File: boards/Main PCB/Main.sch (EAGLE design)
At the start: 98 parts, among them CN1 MINIB, CN2 MINIB, IC1 FT232RL, IC2 FT232RL, J1 3_PIN_JST-XH, J2 2_PIN_JST-XH, Q4 BSS138, Q5 BSS138, Q6 BSS138, Q7 BSS138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

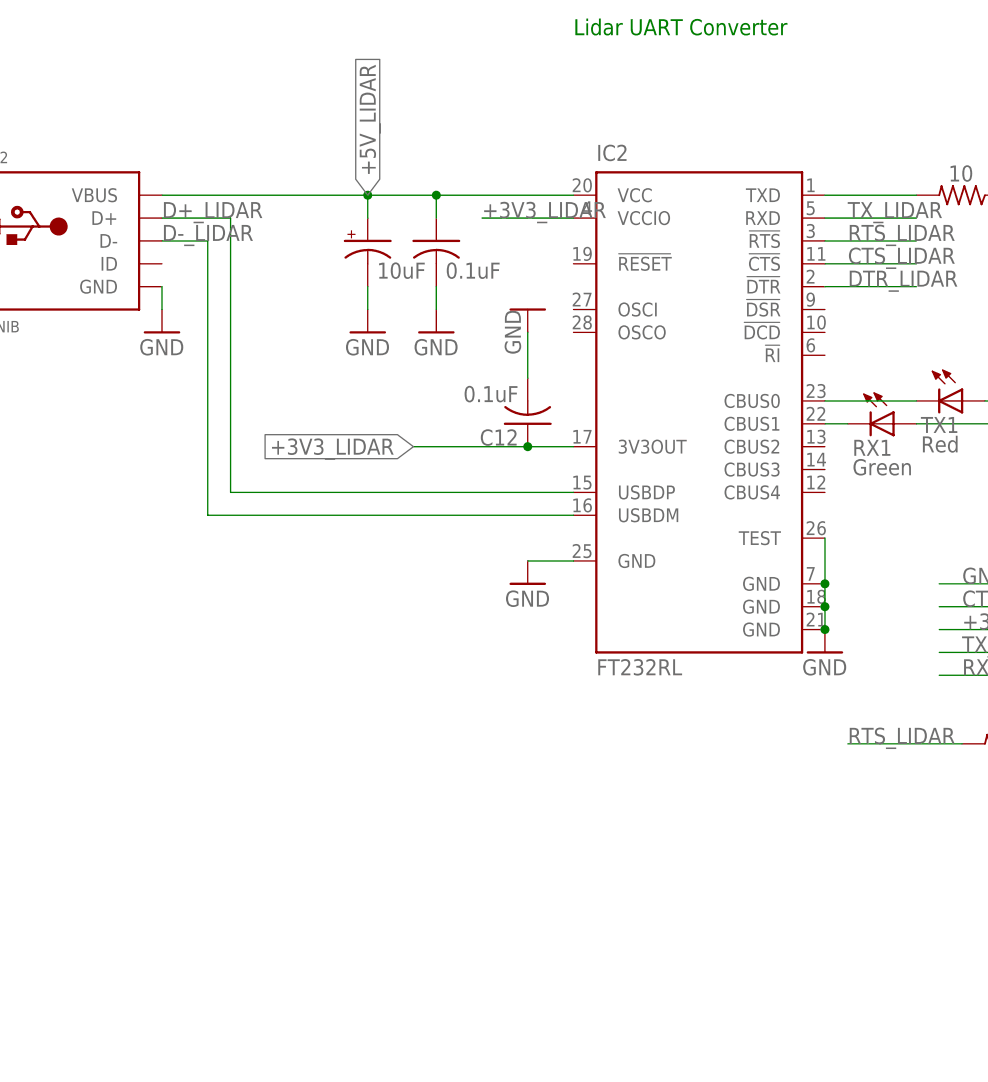
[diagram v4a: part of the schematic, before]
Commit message: Adding diode for lidar protection
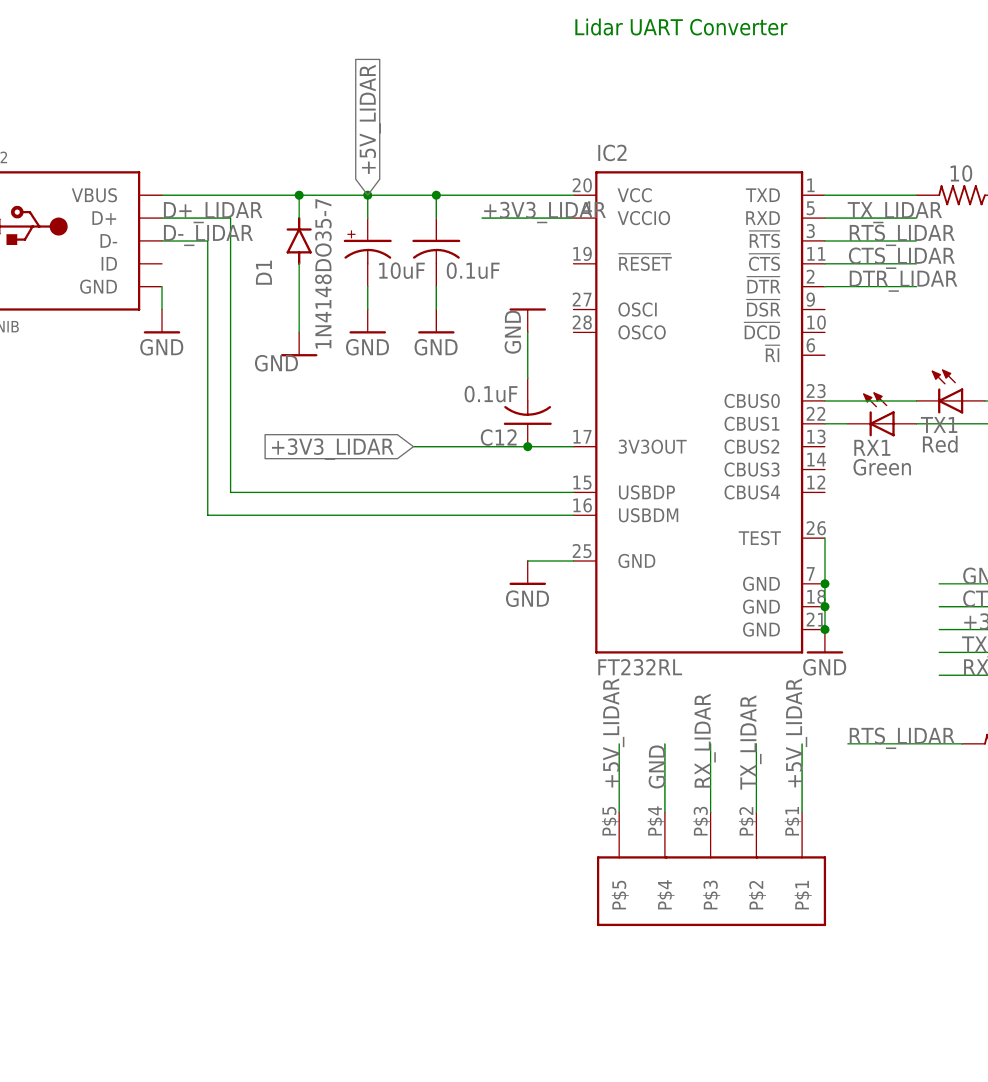
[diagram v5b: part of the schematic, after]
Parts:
- added D1: 1N4148DO35-7, diode:1N4148DO35-7
- added J3: 5_PIN_JST-XH, main_library:5_PIN_JST-XH
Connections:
- net +5V_LIDAR: now also D1.C, J3.P$1, J3.P$5
- net GND: now also D1.A, J3.P$4
- net RX_LIDAR: now also J3.P$3
- net TX_LIDAR: now also J3.P$2
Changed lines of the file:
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@@
 <?xml version="1.0" encoding="utf-8"?>
 <!DOCTYPE eagle SYSTEM "eagle.dtd">
-<eagle version="9.2.2">
+<eagle version="9.3.0">
 <drawing>
 <settings>
@@
 <part name="U$6" library="microbuilder" deviceset="GND" device=""/>
 <part name="R33" library="RESET_FUSE" deviceset="0ZCJ0050FF2G" device=""/>
+<part name="J3" library="main_library" deviceset="5_PIN_JST-XH" device=""/>
+<part name="D1" library="diode" library_urn="urn:adsk.eagle:library:210" deviceset="1N4148" device="DO35-7" package3d_urn="urn:adsk.eagle:package:43339/1"/>
+<part name="GND34" library="supply1" library_urn="urn:adsk.eagle:library:371" deviceset="GND" device=""/>
 </parts>
 <sheets>
@@
 <attribute name="NAME" x="316.23" y="385.0386" size="1.778" layer="95"/>
 <attribute name="VALUE" x="316.23" y="380.238" size="1.778" layer="96"/>
+</instance>
+<instance part="J3" gate="G$1" x="241.3" y="58.42" smashed="yes" rot="R270"/>
+<instance part="D1" gate="G$1" x="195.58" y="129.54" smashed="yes" rot="R90">
+<attribute name="NAME" x="192.5574" y="124.46" size="1.778" layer="95" rot="R90"/>
+<attribute name="VALUE" x="199.1614" y="117.348" size="1.778" layer="96" rot="R90"/>
+</instance>
+<instance part="GND34" gate="1" x="195.58" y="116.84" smashed="yes">
+<attribute name="VALUE" x="195.58" y="116.84" size="1.778" layer="96" rot="R180"/>
 </instance>
 </instances>
@@
 <pinref part="U$6" gate="G$1" pin="GND"/>
 </segment>
+<segment>
+<pinref part="J3" gate="G$1" pin="P$4"/>
+<wire x1="236.22" y1="66.04" x2="236.22" y2="73.66" width="0.1524" layer="91"/>
+<label x="236.22" y="68.58" size="1.778" layer="95" rot="R90"/>
+</segment>
+<segment>
+<pinref part="GND34" gate="1" pin="GND"/>
+<pinref part="D1" gate="G$1" pin="A"/>
+<wire x1="195.58" y1="119.38" x2="195.58" y2="127" width="0.1524" layer="91"/>
+</segment>
 </net>
 <net name="N$36" class="0">
@@
 <wire x1="203.2" y1="132.08" x2="203.2" y2="134.62" width="0.1524" layer="91"/>
 <wire x1="210.82" y1="132.08" x2="210.82" y2="134.62" width="0.1524" layer="91"/>
-<wire x1="203.2" y1="134.62" x2="180.34" y2="134.62" width="0.1524" layer="91"/>
+<wire x1="203.2" y1="134.62" x2="195.58" y2="134.62" width="0.1524" layer="91"/>
 <junction x="203.2" y="134.62"/>
 <junction x="210.82" y="134.62"/>
@@
 <pinref part="CN2" gate="G$1" pin="VBUS"/>
 <label x="203.2" y="134.62" size="1.778" layer="95" rot="R90" xref="yes"/>
+<pinref part="D1" gate="G$1" pin="C"/>
+<wire x1="195.58" y1="134.62" x2="180.34" y2="134.62" width="0.1524" layer="91"/>
+<wire x1="195.58" y1="132.08" x2="195.58" y2="134.62" width="0.1524" layer="91"/>
+<junction x="195.58" y="134.62"/>
+</segment>
+<segment>
+<pinref part="J3" gate="G$1" pin="P$1"/>
+<wire x1="251.46" y1="66.04" x2="251.46" y2="73.66" width="0.1524" layer="91"/>
+<label x="251.46" y="68.58" size="1.778" layer="95" rot="R90"/>
+</segment>
+<segment>
+<pinref part="J3" gate="G$1" pin="P$5"/>
+<wire x1="231.14" y1="66.04" x2="231.14" y2="73.66" width="0.1524" layer="91"/>
+<label x="231.14" y="68.58" size="1.778" layer="95" rot="R90"/>
 </segment>
 </net>
@@
 <pinref part="FTDI1" gate="A" pin="5"/>
 </segment>
+<segment>
+<pinref part="J3" gate="G$1" pin="P$3"/>
+<wire x1="241.3" y1="66.04" x2="241.3" y2="73.66" width="0.1524" layer="91"/>
+<label x="241.3" y="68.58" size="1.778" layer="95" rot="R90"/>
+</segment>
 </net>
 <net name="TX_LIDAR" class="0">
@@
 <pinref part="FTDI1" gate="A" pin="4"/>
 </segment>
-</net>
+<segment>
+<pinref part="J3" gate="G$1" pin="P$2"/>
+<wire x1="246.38" y1="66.04" x2="246.38" y2="73.66" width="0.1524" layer="91"/>
+<label x="246.38" y="68.58" size="1.778" layer="95" rot="R90"/>
+</segment>
+</net>

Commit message: Fixing trace widths and net names
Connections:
- net N$11 renamed CAP
- net N$13 renamed LED
- net N$34 renamed BOOT0
- net N$43 renamed RESET
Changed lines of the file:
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@@
 <?xml version="1.0" encoding="utf-8"?>
 <!DOCTYPE eagle SYSTEM "eagle.dtd">
-<eagle version="9.3.0">
+<eagle version="9.2.2">
 <drawing>
 <settings>
@@
 </segment>
 </net>
-<net name="N$34" class="0">
+<net name="BOOT0" class="0">
 <segment>
 <pinref part="U2" gate="G$1" pin="BOOT0"/>
@@
 </segment>
 </net>
-<net name="N$43" class="0">
+<net name="RESET" class="0">
 <segment>
 <wire x1="220.98" y1="297.18" x2="220.98" y2="325.12" width="0.1524" layer="91"/>
@@
 </segment>
 </net>
-<net name="N$13" class="0">
+<net name="LED" class="0">
 <segment>
 <pinref part="RX2" gate="G$1" pin="C"/>
@@
 </segment>
 </net>
-<net name="N$11" class="0">
+<net name="CAP" class="0">
 <segment>
 <pinref part="U$3" gate="G$1" pin="CAP"/>

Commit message: AAdding decoupling capacitors for design review
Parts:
- added C18, C19, C26, C27, C28, C29: .1uF, rcl:C-USC0805
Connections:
- net +3V3: now also C28.1, C29.1
- net +5V: now also C18.1, C19.1, C26.1, C27.1
- net GND: now also C18.2, C19.2, C26.2, C27.2, C28.2, C29.2
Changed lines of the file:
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@@
 <part name="D1" library="diode" library_urn="urn:adsk.eagle:library:210" deviceset="1N4148" device="DO35-7" package3d_urn="urn:adsk.eagle:package:43339/1"/>
 <part name="GND34" library="supply1" library_urn="urn:adsk.eagle:library:371" deviceset="GND" device=""/>
+<part name="C18" library="rcl" library_urn="urn:adsk.eagle:library:334" deviceset="C-US" device="C0805" package3d_urn="urn:adsk.eagle:package:23617/2" value=".1uF"/>
+<part name="C19" library="rcl" library_urn="urn:adsk.eagle:library:334" deviceset="C-US" device="C0805" package3d_urn="urn:adsk.eagle:package:23617/2" value=".1uF"/>
+<part name="C26" library="rcl" library_urn="urn:adsk.eagle:library:334" deviceset="C-US" device="C0805" package3d_urn="urn:adsk.eagle:package:23617/2" value=".1uF"/>
+<part name="C28" library="rcl" library_urn="urn:adsk.eagle:library:334" deviceset="C-US" device="C0805" package3d_urn="urn:adsk.eagle:package:23617/2" value=".1uF"/>
+<part name="C29" library="rcl" library_urn="urn:adsk.eagle:library:334" deviceset="C-US" device="C0805" package3d_urn="urn:adsk.eagle:package:23617/2" value=".1uF"/>
+<part name="GND35" library="supply1" library_urn="urn:adsk.eagle:library:371" deviceset="GND" device=""/>
+<part name="GND36" library="supply1" library_urn="urn:adsk.eagle:library:371" deviceset="GND" device=""/>
+<part name="GND37" library="supply1" library_urn="urn:adsk.eagle:library:371" deviceset="GND" device=""/>
+<part name="GND38" library="supply1" library_urn="urn:adsk.eagle:library:371" deviceset="GND" device=""/>
+<part name="GND39" library="supply1" library_urn="urn:adsk.eagle:library:371" deviceset="GND" device=""/>
+<part name="C27" library="rcl" library_urn="urn:adsk.eagle:library:334" deviceset="C-US" device="C0805" package3d_urn="urn:adsk.eagle:package:23617/2" value=".1uF"/>
+<part name="GND40" library="supply1" library_urn="urn:adsk.eagle:library:371" deviceset="GND" device=""/>
 </parts>
 <sheets>
@@
 <instance part="GND34" gate="1" x="195.58" y="116.84" smashed="yes">
 <attribute name="VALUE" x="195.58" y="116.84" size="1.778" layer="96" rot="R180"/>
+</instance>
+<instance part="C18" gate="G$1" x="45.72" y="360.68" smashed="yes" rot="R270">
+<attribute name="VALUE" x="41.529" y="359.664" size="1.778" layer="96" rot="R270"/>
+</instance>
+<instance part="C19" gate="G$1" x="45.72" y="312.42" smashed="yes" rot="R270">
+<attribute name="VALUE" x="41.529" y="311.404" size="1.778" layer="96" rot="R270"/>
+</instance>
+<instance part="C26" gate="G$1" x="45.72" y="266.7" smashed="yes" rot="R270">
+<attribute name="VALUE" x="41.529" y="265.684" size="1.778" layer="96" rot="R270"/>
+</instance>
+<instance part="C28" gate="G$1" x="480.06" y="312.42" smashed="yes" rot="R90">
+<attribute name="VALUE" x="484.251" y="313.436" size="1.778" layer="96" rot="R90"/>
+</instance>
+<instance part="C29" gate="G$1" x="480.06" y="335.28" smashed="yes" rot="R90">
+<attribute name="VALUE" x="484.251" y="336.296" size="1.778" layer="96" rot="R90"/>
+</instance>
+<instance part="GND35" gate="1" x="35.56" y="266.7" smashed="yes" rot="R270">
+<attribute name="VALUE" x="33.02" y="269.24" size="1.778" layer="96" rot="R270"/>
+</instance>
+<instance part="GND36" gate="1" x="35.56" y="312.42" smashed="yes" rot="R270">
+<attribute name="VALUE" x="33.02" y="314.96" size="1.778" layer="96" rot="R270"/>
+</instance>
+<instance part="GND37" gate="1" x="35.56" y="360.68" smashed="yes" rot="R270">
+<attribute name="VALUE" x="33.02" y="363.22" size="1.778" layer="96" rot="R270"/>
+</instance>
+<instance part="GND38" gate="1" x="490.22" y="335.28" smashed="yes" rot="R90">
+<attribute name="VALUE" x="492.76" y="332.74" size="1.778" layer="96" rot="R90"/>
+</instance>
+<instance part="GND39" gate="1" x="490.22" y="312.42" smashed="yes" rot="R90">
+<attribute name="VALUE" x="492.76" y="309.88" size="1.778" layer="96" rot="R90"/>
+</instance>
+<instance part="C27" gate="G$1" x="528.32" y="261.62" smashed="yes" rot="R180">
+<attribute name="VALUE" x="527.304" y="265.811" size="1.778" layer="96" rot="R180"/>
+</instance>
+<instance part="GND40" gate="1" x="533.4" y="266.7" smashed="yes" rot="R90">
+<attribute name="VALUE" x="535.94" y="264.16" size="1.778" layer="96" rot="R90"/>
 </instance>
 </instances>
@@
 <pinref part="X6" gate="-1" pin="S"/>
 <wire x1="462.28" y1="330.2" x2="467.36" y2="330.2" width="0.1524" layer="91"/>
+<pinref part="C29" gate="G$1" pin="1"/>
+<wire x1="467.36" y1="330.2" x2="467.36" y2="335.28" width="0.1524" layer="91"/>
+<wire x1="467.36" y1="335.28" x2="477.52" y2="335.28" width="0.1524" layer="91"/>
+<junction x="467.36" y="330.2"/>
 </segment>
 <segment>
@@
 <pinref part="X7" gate="-1" pin="S"/>
 <wire x1="462.28" y1="307.34" x2="467.36" y2="307.34" width="0.1524" layer="91"/>
+<pinref part="C28" gate="G$1" pin="1"/>
+<wire x1="467.36" y1="307.34" x2="467.36" y2="312.42" width="0.1524" layer="91"/>
+<wire x1="467.36" y1="312.42" x2="477.52" y2="312.42" width="0.1524" layer="91"/>
+<junction x="467.36" y="307.34"/>
 </segment>
 <segment>
@@
 <wire x1="195.58" y1="119.38" x2="195.58" y2="127" width="0.1524" layer="91"/>
 </segment>
+<segment>
+<pinref part="GND37" gate="1" pin="GND"/>
+<pinref part="C18" gate="G$1" pin="2"/>
+<wire x1="38.1" y1="360.68" x2="40.64" y2="360.68" width="0.1524" layer="91"/>
+</segment>
+<segment>
+<pinref part="GND36" gate="1" pin="GND"/>
+<pinref part="C19" gate="G$1" pin="2"/>
+<wire x1="38.1" y1="312.42" x2="40.64" y2="312.42" width="0.1524" layer="91"/>
+</segment>
+<segment>
+<pinref part="GND35" gate="1" pin="GND"/>
+<pinref part="C26" gate="G$1" pin="2"/>
+<wire x1="38.1" y1="266.7" x2="40.64" y2="266.7" width="0.1524" layer="91"/>
+</segment>
+<segment>
+<pinref part="C29" gate="G$1" pin="2"/>
+<pinref part="GND38" gate="1" pin="GND"/>
+<wire x1="485.14" y1="335.28" x2="487.68" y2="335.28" width="0.1524" layer="91"/>
+</segment>
+<segment>
+<pinref part="C28" gate="G$1" pin="2"/>
+<pinref part="GND39" gate="1" pin="GND"/>
+<wire x1="485.14" y1="312.42" x2="487.68" y2="312.42" width="0.1524" layer="91"/>
+</segment>
+<segment>
+<pinref part="C27" gate="G$1" pin="2"/>
+<pinref part="GND40" gate="1" pin="GND"/>
+<wire x1="528.32" y1="266.7" x2="530.86" y2="266.7" width="0.1524" layer="91"/>
+</segment>
 </net>
 <net name="N$36" class="0">
@@
 <pinref part="R28" gate="G$1" pin="2"/>
 <wire x1="66.04" y1="365.76" x2="66.04" y2="360.68" width="0.1524" layer="91"/>
-<wire x1="53.34" y1="365.76" x2="53.34" y2="350.52" width="0.1524" layer="91"/>
+<wire x1="53.34" y1="365.76" x2="53.34" y2="360.68" width="0.1524" layer="91"/>
 <junction x="53.34" y="365.76"/>
+<wire x1="53.34" y1="360.68" x2="53.34" y2="350.52" width="0.1524" layer="91"/>
 <wire x1="53.34" y1="350.52" x2="50.8" y2="350.52" width="0.1524" layer="91"/>
 <pinref part="X3" gate="-4" pin="S"/>
 <pinref part="P+3" gate="1" pin="+5V"/>
+<pinref part="C18" gate="G$1" pin="1"/>
+<wire x1="48.26" y1="360.68" x2="53.34" y2="360.68" width="0.1524" layer="91"/>
+<junction x="53.34" y="360.68"/>
 </segment>
 <segment>
@@
 <pinref part="R24" gate="G$1" pin="2"/>
 <wire x1="66.04" y1="271.78" x2="66.04" y2="266.7" width="0.1524" layer="91"/>
-<wire x1="53.34" y1="271.78" x2="53.34" y2="256.54" width="0.1524" layer="91"/>
+<wire x1="53.34" y1="271.78" x2="53.34" y2="266.7" width="0.1524" layer="91"/>
 <junction x="53.34" y="271.78"/>
+<wire x1="53.34" y1="266.7" x2="53.34" y2="256.54" width="0.1524" layer="91"/>
 <wire x1="53.34" y1="256.54" x2="50.8" y2="256.54" width="0.1524" layer="91"/>
 <pinref part="X4" gate="-4" pin="S"/>
 <pinref part="P+4" gate="1" pin="+5V"/>
+<pinref part="C26" gate="G$1" pin="1"/>
+<wire x1="48.26" y1="266.7" x2="53.34" y2="266.7" width="0.1524" layer="91"/>
+<junction x="53.34" y="266.7"/>
 </segment>
 <segment>
@@
 <pinref part="R12" gate="G$1" pin="2"/>
 <wire x1="66.04" y1="317.5" x2="66.04" y2="312.42" width="0.1524" layer="91"/>
-<wire x1="53.34" y1="317.5" x2="53.34" y2="302.26" width="0.1524" layer="91"/>
+<wire x1="53.34" y1="317.5" x2="53.34" y2="312.42" width="0.1524" layer="91"/>
 <junction x="53.34" y="317.5"/>
 <pinref part="X5" gate="-4" pin="S"/>
+<wire x1="53.34" y1="312.42" x2="53.34" y2="302.26" width="0.1524" layer="91"/>
 <wire x1="53.34" y1="302.26" x2="50.8" y2="302.26" width="0.1524" layer="91"/>
 <pinref part="P+5" gate="1" pin="+5V"/>
+<pinref part="C19" gate="G$1" pin="1"/>
+<wire x1="48.26" y1="312.42" x2="53.34" y2="312.42" width="0.1524" layer="91"/>
+<junction x="53.34" y="312.42"/>
 </segment>
 <segment>
@@
 <label x="533.4" y="256.54" size="1.27" layer="95" rot="R90" xref="yes"/>
 <wire x1="533.4" y1="246.38" x2="533.4" y2="256.54" width="0.1524" layer="91"/>
-</segment>
-<segment>
+<pinref part="C27" gate="G$1" pin="1"/>
+<wire x1="528.32" y1="259.08" x2="528.32" y2="256.54" width="0.1524" layer="91"/>
+<wire x1="528.32" y1="256.54" x2="533.4" y2="256.54" width="0.1524" layer="91"/>
+</segment>
+<segment>
